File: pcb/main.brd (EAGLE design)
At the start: 160 x 100 mm, 45 parts, among them IC1 FT230XS, J3 455-1750-1-ND, J6 M1 connector, J7 M2 connector, Q1 2.5A/30V/105mΩ, U1 LSM303C, U2 ESP-WROOM-32

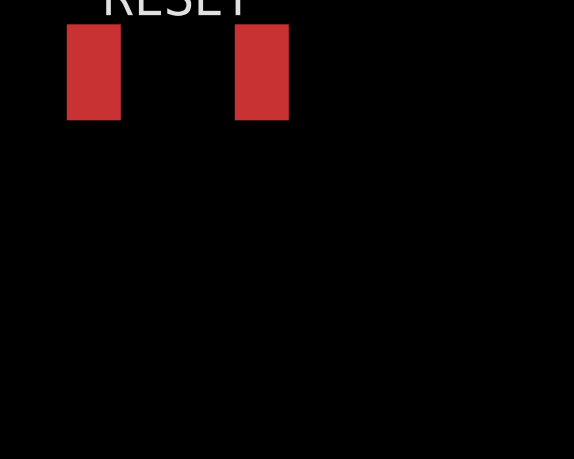
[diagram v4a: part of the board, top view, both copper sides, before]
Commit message: mosfet for laser
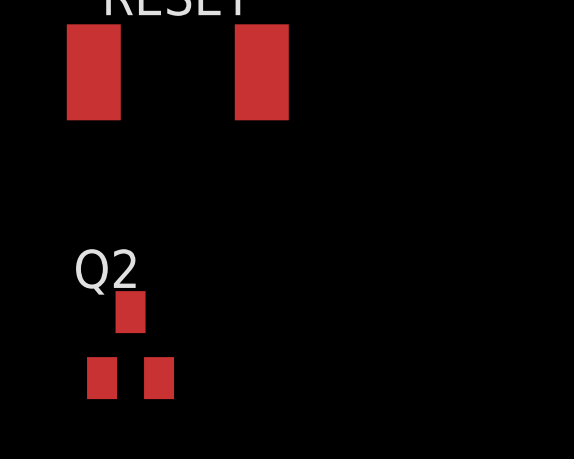
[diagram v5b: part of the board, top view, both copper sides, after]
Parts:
- added Q2: (no value), adafruit:SOT23
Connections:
- new net N$10: J2.1, Q2.3
- net 5V: now also J2.2
- net GND: now also Q2.2; no longer J2.1
- net PWM_LASER: now also Q2.1; no longer J2.2
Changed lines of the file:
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@@
 <element name="CN1" library="adafruit" library_urn="urn:adsk.eagle:library:420" package="USB-MINIB" value="" x="-101.9556" y="-131.8768"/>
 <element name="RESET" library="DiscreteComponents" package="SW_2512" value="" x="-103.4288" y="-144.0688"/>
+<element name="Q2" library="adafruit" library_urn="urn:adsk.eagle:library:420" package="SOT23" value="" x="-105.0036" y="-153.162"/>
 </elements>
 <signals>
@@
 <contactref element="J3" pad="3"/>
 <contactref element="J1" pad="1"/>
-<contactref element="J2" pad="1"/>
 <contactref element="D2" pad="C"/>
 <contactref element="R1" pad="1"/>
@@
 <contactref element="CN1" pad="GND"/>
 <contactref element="RESET" pad="2"/>
+<contactref element="Q2" pad="2"/>
+<wire x1="-104.0536" y1="-154.262" x2="-100.6288" y2="-144.0688" width="0" layer="19" extent="1-1"/>
 <wire x1="-100.3556" y1="-127.8128" x2="-100.6288" y2="-144.0688" width="0" layer="19" extent="1-1"/>
 <wire x1="-91.86" y1="-117.348" x2="-100.3556" y2="-127.8128" width="0" layer="19" extent="1-1"/>
@@
 <wire x1="-33.413" y1="53.34" x2="-30.48" y2="49.53" width="0" layer="19" extent="1-1"/>
 <wire x1="-36.83" y1="49.53" x2="-33.413" y2="53.34" width="0" layer="19" extent="1-1"/>
-<wire x1="-24.13" y1="49.53" x2="-30.48" y2="49.53" width="0" layer="19" extent="1-1"/>
-<wire x1="-17.78" y1="49.53" x2="-24.13" y2="49.53" width="0" layer="19" extent="1-1"/>
+<wire x1="-46.14" y1="49.53" x2="-36.83" y2="49.53" width="0" layer="19" extent="1-1"/>
+<wire x1="-20.0914" y1="40.0812" x2="-30.775" y2="38.985" width="0" layer="19" extent="1-1"/>
+<wire x1="-21.59" y1="33.02" x2="-20.0914" y2="40.0812" width="0" layer="19" extent="1-1"/>
+<wire x1="-17.78" y1="49.53" x2="-20.0914" y2="40.0812" width="0" layer="19" extent="1-1"/>
 <wire x1="-19.9" y1="54.61" x2="-17.78" y2="49.53" width="0" layer="19" extent="1-1"/>
 <wire x1="-14.39" y1="54.61" x2="-19.9" y2="54.61" width="0" layer="19" extent="1-1"/>
-<wire x1="-46.14" y1="49.53" x2="-36.83" y2="49.53" width="0" layer="19" extent="1-1"/>
-<wire x1="-20.0914" y1="40.0812" x2="-17.78" y2="49.53" width="0" layer="19" extent="1-1"/>
-<wire x1="-21.59" y1="33.02" x2="-20.0914" y2="40.0812" width="0" layer="19" extent="1-1"/>
 <wire x1="-21.59" y1="23.12" x2="-21.59" y2="33.02" width="0" layer="19" extent="1-1"/>
 <wire x1="-18.19" y1="23.12" x2="-21.59" y2="23.12" width="0" layer="19" extent="1-1"/>
@@
 </signal>
 <signal name="PWM_LASER">
-<contactref element="J2" pad="2"/>
+<contactref element="Q2" pad="1"/>
 </signal>
 <signal name="5V">
@@
 <contactref element="U$1" pad="2"/>
 <contactref element="U$1" pad="4"/>
-<wire x1="-17.78" y1="46.279" x2="-16.09" y2="54.61" width="0" layer="19" extent="1-1"/>
+<contactref element="J2" pad="2"/>
+<wire x1="-21.59" y1="49.53" x2="-16.09" y2="54.61" width="0" layer="19" extent="1-1"/>
+<wire x1="-17.78" y1="46.279" x2="-21.59" y2="49.53" width="0" layer="19" extent="1-1"/>
 <wire x1="-17.78" y1="40.0812" x2="-17.78" y2="46.279" width="0" layer="19" extent="1-1"/>
-<wire x1="-39.37" y1="40.64" x2="-17.78" y2="40.0812" width="0" layer="19" extent="1-1"/>
+<wire x1="-39.37" y1="40.64" x2="-21.59" y2="49.53" width="0" layer="19" extent="1-1"/>
 </signal>
 <signal name="PWM_SERVO">
@@
 <contactref element="IC1" pad="6"/>
 </signal>
+<signal name="N$10">
+<contactref element="Q2" pad="3"/>
+<contactref element="J2" pad="1"/>
+<wire x1="-105.0036" y1="-152.062" x2="-24.13" y2="49.53" width="0" layer="19" extent="1-1"/>
+</signal>
 </signals>

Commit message: wired up almost all of esp's peripherals
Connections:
- new net ADC_PHOTO: J4.2, R3.1, U2.35
- new net N$16: U2.26
- new net RST: U2.3
- new net TCK: U2.16
- new net TDI: U2.14
- new net TDO: U2.23
- new net TMS: U2.13
- net M1+: now also U2.8
- net M1-: now also U2.9
- net M2+: now also U2.10
- net M2-: now also U2.11
- net N$4: now also U2.25; no longer J4.2, R3.1
- net PWM_LASER: now also U2.24
- net PWM_LED: now also U2.34
- net PWM_SERVO: now also U2.12
- net SCL: now also U2.36
- net SDA: now also U2.33
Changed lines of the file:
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@@
 <?xml version="1.0" encoding="utf-8"?>
 <!DOCTYPE eagle SYSTEM "eagle.dtd">
-<eagle version="8.3.2">
+<eagle version="8.6.0">
 <drawing>
 <settings>
@@
 <param name="dpMaxLengthDifference" value="10mm"/>
 <param name="dpGapFactor" value="2.5"/>
-<param name="checkGrid" value="0"/>
 <param name="checkAngle" value="0"/>
 <param name="checkFont" value="1"/>
 <param name="checkRestrict" value="1"/>
+<param name="checkStop" value="0"/>
+<param name="checkValues" value="0"/>
 <param name="useDiameter" value="13"/>
 <param name="maxErrors" value="50"/>
@@
 </element>
 <element name="J8" library="electricSheepParty" package="1X02" value="" x="-87.0204" y="-129.3368">
-<attribute name="COMM" value="Photo Receptor" x="-87.0204" y="-129.3368" size="1.778" layer="27" display="off"/>
+<attribute name="COMM" value="IMU Interrupt Header" x="-87.0204" y="-129.3368" size="1.778" layer="27" display="off"/>
 </element>
 <element name="CN1" library="adafruit" library_urn="urn:adsk.eagle:library:420" package="USB-MINIB" value="" x="-101.9556" y="-131.8768"/>
@@
 <signal name="PWM_LASER">
 <contactref element="Q2" pad="1"/>
+<contactref element="U2" pad="24"/>
+<wire x1="-105.9536" y1="-154.262" x2="-77.9376" y2="-98.7276" width="0" layer="19" extent="1-1"/>
 </signal>
 <signal name="5V">
@@
 <signal name="PWM_SERVO">
 <contactref element="J3" pad="1"/>
+<contactref element="U2" pad="12"/>
+<wire x1="-41.91" y1="40.64" x2="-92.9176" y2="-94.4476" width="0" layer="19" extent="1-1"/>
 </signal>
 <signal name="N$1">
@@
 <wire x1="-35.167" y1="53.34" x2="-23.71" y2="54.61" width="0" layer="19" extent="1-1"/>
 </signal>
-<signal name="N$4">
+<signal name="ADC_PHOTO">
 <contactref element="J4" pad="2"/>
 <contactref element="R3" pad="1"/>
-<wire x1="-27.94" y1="49.53" x2="-27.52" y2="54.61" width="0" layer="19" extent="1-1"/>
+<contactref element="U2" pad="35"/>
+<wire x1="-27.94" y1="49.53" x2="-74.4176" y2="-84.2876" width="0" layer="19" extent="1-1"/>
+<wire x1="-27.52" y1="54.61" x2="-27.94" y2="49.53" width="0" layer="19" extent="1-1"/>
 </signal>
 <signal name="N$5">
@@
 <signal name="PWM_LED">
 <contactref element="R4" pad="2"/>
+<contactref element="U2" pad="34"/>
+<wire x1="-29.63" y1="54.61" x2="-74.4176" y2="-85.5576" width="0" layer="19" extent="1-1"/>
 </signal>
 <signal name="3V3">
@@
 <contactref element="U$2" pad="2"/>
 <contactref element="J6" pad="2"/>
+<contactref element="U2" pad="8"/>
+<wire x1="-39.37" y1="-30.48" x2="-92.9176" y2="-89.3676" width="0" layer="19" extent="1-1"/>
 <wire x1="-33.375" y1="38.985" x2="-39.37" y2="-30.48" width="0" layer="19" extent="1-1"/>
 </signal>
@@
 <contactref element="U$2" pad="4"/>
 <contactref element="J6" pad="1"/>
+<contactref element="U2" pad="9"/>
+<wire x1="-41.91" y1="-30.48" x2="-92.9176" y2="-90.6376" width="0" layer="19" extent="1-1"/>
 <wire x1="-32.075" y1="38.985" x2="-41.91" y2="-30.48" width="0" layer="19" extent="1-1"/>
 </signal>
@@
 <contactref element="U$2" pad="7"/>
 <contactref element="J7" pad="2"/>
+<contactref element="U2" pad="10"/>
+<wire x1="-39.37" y1="-49.53" x2="-92.9176" y2="-91.9076" width="0" layer="19" extent="1-1"/>
 <wire x1="-30.125" y1="38.985" x2="-39.37" y2="-49.53" width="0" layer="19" extent="1-1"/>
 </signal>
@@
 <contactref element="U$2" pad="5"/>
 <contactref element="J7" pad="1"/>
+<contactref element="U2" pad="11"/>
+<wire x1="-41.91" y1="-49.53" x2="-92.9176" y2="-93.1776" width="0" layer="19" extent="1-1"/>
 <wire x1="-31.425" y1="38.985" x2="-41.91" y2="-49.53" width="0" layer="19" extent="1-1"/>
 </signal>
@@
 <signal name="SCL">
 <contactref element="U1" pad="1"/>
+<contactref element="U2" pad="36"/>
+<wire x1="-74.4176" y1="-83.0176" x2="-70.6508" y2="-98.8688" width="0" layer="19" extent="1-1"/>
 </signal>
 <signal name="SDA">
 <contactref element="U1" pad="4"/>
+<contactref element="U2" pad="33"/>
+<wire x1="-74.4176" y1="-86.8276" x2="-70.6508" y2="-100.3688" width="0" layer="19" extent="1-1"/>
 </signal>
 <signal name="N$12">
@@
 <wire x1="-105.0036" y1="-152.062" x2="-24.13" y2="49.53" width="0" layer="19" extent="1-1"/>
 </signal>
+<signal name="TDI">
+<contactref element="U2" pad="14"/>
+</signal>
+<signal name="TMS">
+<contactref element="U2" pad="13"/>
+</signal>
+<signal name="TDO">
+<contactref element="U2" pad="23"/>
+</signal>
+<signal name="TCK">
+<contactref element="U2" pad="16"/>
+</signal>
+<signal name="RST">
+<contactref element="U2" pad="3"/>
+</signal>
+<signal name="N$16">
+<contactref element="U2" pad="26"/>
+</signal>
+<signal name="N$4">
+<contactref element="U2" pad="25"/>
+</signal>
 </signals>

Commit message: more esp pins and isolating grounds
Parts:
- removed CN1: (no value), adafruit:USB-MINIB
- removed IC1: FT230XS, electricSheepParty:SSOP16
- removed J8: (no value), electricSheepParty:1X02
- removed RESET: (no value), DiscreteComponents:SW_2512
- added C15: 10uF, rcl:C0805
- added C16, C17: 1nF, electricSheepParty:0603
- added C18, C20: 100uF, eagle-ltspice:C1206
- added C19: 1uF, electricSheepParty:0603
- added FB1: (no value), rcl:R0603
- added R10: 470, electricSheepParty:0603
- added R8: 20k, electricSheepParty:0603
- added R9: 10k, electricSheepParty:0603
- added RESET1: S2, DiscreteComponents:SW_2512
- C14: device electricSheepParty:0603 -> rcl:C0805
- C3, C5: device rcl:C0603 -> rcl:C0805
- R1: value 100k -> 1M
- R3, R5: value (none) -> 10k
- R4: value (none) -> 470
- moved R4 260.5 mm to (-121.8, -189.4)
- moved C3 180.2 mm to (-105.4, -178.5)
- moved C5 176.4 mm to (-105.4, -184.7)
- moved D1 72.7 mm to (22.6, 15.9)
- moved C14 56.5 mm to (-105.4, -172.4)
- moved Q1 55.8 mm to (22.6, 13.4), turned to 180 degrees
- moved R1 48.6 mm to (15.9, 20.8)
- moved J1 47.3 mm to (12.4, 13.1), turned to 270 degrees
- moved S1 46.2 mm to (16.5, 4.27), turned to 270 degrees
- renumbered U2 to U5
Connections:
- net N$4 renamed IO0
- removed net CTS: IC1.6
- removed net D+: CN1.D+, IC1.8
- removed net D-: CN1.D-, IC1.9
- removed net RESET: IC1.11, RESET.1
- removed net RST: U5.3
- removed net RTS: IC1.2
- removed net RX: IC1.4
- removed net TX: IC1.1
- new net 1/3_BAT: R8.1, R9.2, U5.4
- new net 6V_RAW: J1.2, S1.P$2
- new net AGND: C1.2, C10.-, C11.2, C15.1, C2.2, C20.2, C3.2, C4.2, C6.2, C7.2, C8.2, C9.-, D2.C, D3.1, FB1.1, J1.1, J3.3, Q2.2, R1.1, R9.1, U$1.1, U$2.13, U$2.17, U$2.3, U$2.6, U$3.3, U$3.5, U$3.6
- new net EN: C17.1, R10.2, R4.2, U5.3
- new net N$11: C16.1, R4.1, RESET1.1
- new net N$14: U5.7
- new net N$15: U5.20
- new net N$17: U5.21
- new net N$18: U5.22
- new net N$19: U5.27
- new net N$23: U5.31
- new net N$24: U5.37
- new net N$4: U5.5
- new net PHOTO: U5.35
- net 3V3: now also C20.1, C5.1, R10.1; no longer C5.2, CN1.VBUS, IC1.10, IC1.12, IC1.3, U5.2
- net 5V: now also C15.2
- net 6V: now also D1.C, Q1.2, R2.2, R8.2
- net ADC_PHOTO: no longer U5.35
- net GND: now also C16.2, C17.2, C18.2, C19.2, FB1.2, RESET1.2; no longer C1.2, C10.-, C11.2, C2.2, C3.2, C4.2, C6.2, C7.2, C8.2, C9.-, CN1.GND, D2.C, D3.1, IC1.13, IC1.5, J1.1, J3.3, Q2.2, R1.1, RESET.2, U$1.1, U$2.13, U$2.17, U$2.3, U$2.6, U$3.3, U$3.5, U$3.6
- net INT_MAG: now also U5.29; no longer J8.1
- net INT_XL: now also U5.30; no longer J8.2
- net M1+: no longer U5.8
- net M1-: no longer U5.9
- net M2+: no longer U5.10
- net M2-: no longer U5.11
- net MAG_RDY: now also U5.28
- net N$5: now also U5.6; no longer J5.2, R4.1
- net N$9: now also C5.2; no longer C5.1
- net PWM_LED: now also J5.2; no longer R4.2
- net PWM_M1A: now also U5.8
- net PWM_M1B: now also U5.9
- net PWM_M2A: now also U5.11
- net PWM_M2B: now also U5.10
- net VCC: now also C18.1, C19.1, U5.2; no longer D1.C, J1.2, Q1.2, R2.2, S1.P$2
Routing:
- added copper zone on layer 1, net 6V_RAW
- added copper zone on layer 1, net N$3

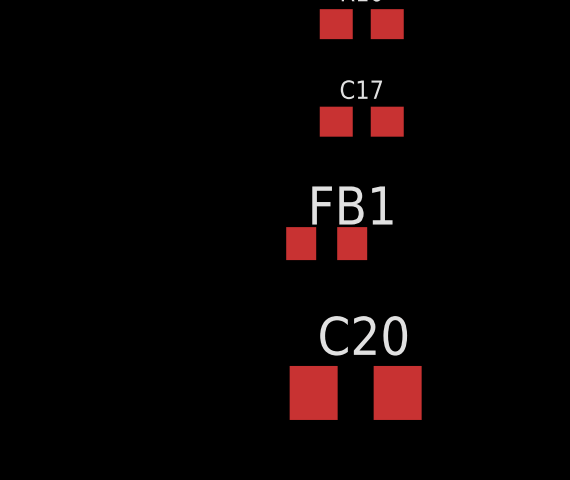
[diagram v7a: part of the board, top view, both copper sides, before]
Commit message: added schmitt trigger
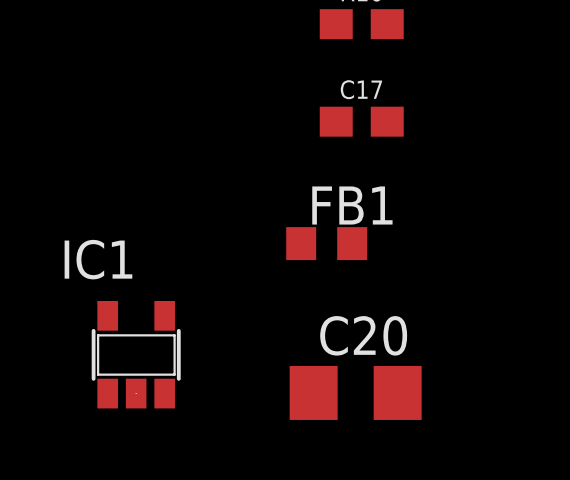
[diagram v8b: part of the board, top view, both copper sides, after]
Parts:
- added IC1: NC7SZ14M5X, electricSheepParty:SOT23-5
- R3: value 10k -> 8.2k
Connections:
- net ADC_PHOTO: now also IC1.2
- net GND: now also IC1.3
- net PHOTO: now also IC1.4
- net VCC: now also IC1.5
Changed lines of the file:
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@@
 <?xml version="1.0" encoding="utf-8"?>
 <!DOCTYPE eagle SYSTEM "eagle.dtd">
-<eagle version="8.3.2">
+<eagle version="8.6.0">
 <drawing>
 <settings>
@@
 <param name="dpMaxLengthDifference" value="10mm"/>
 <param name="dpGapFactor" value="2.5"/>
-<param name="checkGrid" value="0"/>
 <param name="checkAngle" value="0"/>
 <param name="checkFont" value="1"/>
 <param name="checkRestrict" value="1"/>
+<param name="checkStop" value="0"/>
+<param name="checkValues" value="0"/>
 <param name="useDiameter" value="13"/>
 <param name="maxErrors" value="50"/>
@@
 <attribute name="PROD_ID" value=" " x="-22.86" y="54.61" size="1.778" layer="27" display="off"/>
 </element>
-<element name="R3" library="electricSheepParty" package="0603" value="10k" x="-26.67" y="54.61">
+<element name="R3" library="electricSheepParty" package="0603" value="8.2k" x="-26.67" y="54.61">
 <attribute name="PROD_ID" value=" " x="-26.67" y="54.61" size="1.778" layer="27" display="off"/>
 </element>
@@
 <attribute name="SPICEPREFIX" value="C" x="-121.9708" y="-224.028" size="1.778" layer="27" display="off"/>
 </element>
+<element name="IC1" library="electricSheepParty" package="SOT23-5" value="NC7SZ14M5X" x="-129.286" y="-222.758"/>
 </elements>
 <signals>
@@
 <contactref element="C17" pad="2"/>
 <contactref element="FB1" pad="2"/>
+<contactref element="IC1" pad="3"/>
 <wire x1="-91.86" y1="-110.8456" x2="-91.86" y2="-114.0968" width="0" layer="19" extent="1-1"/>
 <wire x1="-93.56" y1="-104.3432" x2="-91.86" y2="-110.8456" width="0" layer="19" extent="1-1"/>
@@
 <wire x1="-120.9176" y1="-214.9856" x2="-120.9176" y2="-208.4832" width="0" layer="19" extent="1-1"/>
 <wire x1="-122.086" y1="-219.0496" x2="-120.9176" y2="-214.9856" width="0" layer="19" extent="1-1"/>
+<wire x1="-128.336" y1="-224.048" x2="-122.086" y2="-219.0496" width="0" layer="19" extent="1-1"/>
 <wire x1="-36.83" y1="49.53" x2="-74.4176" y2="-80.4776" width="0" layer="19" extent="1-1"/>
 <wire x1="-30.48" y1="49.53" x2="-36.83" y2="49.53" width="0" layer="19" extent="1-1"/>
@@
 <contactref element="J4" pad="2"/>
 <contactref element="R3" pad="1"/>
-<wire x1="-27.94" y1="49.53" x2="-27.52" y2="54.61" width="0" layer="19" extent="1-1"/>
+<contactref element="IC1" pad="2"/>
+<wire x1="-27.94" y1="49.53" x2="-129.286" y2="-224.048" width="0" layer="19" extent="1-1"/>
+<wire x1="-27.52" y1="54.61" x2="-27.94" y2="49.53" width="0" layer="19" extent="1-1"/>
 </signal>
 <signal name="PWM_LED">
@@
 <vertex x="9.8044" y="11.7348"/>
 </polygon>
+<wire x1="16.4592" y1="4.2672" x2="12.3952" y2="10.5664" width="0" layer="19" extent="1-1"/>
 </signal>
 <signal name="1/3_BAT">
@@
 <contactref element="C18" pad="1"/>
 <contactref element="C19" pad="1"/>
+<contactref element="IC1" pad="5"/>
 <wire x1="-123.3708" y1="-203.8096" x2="-92.9176" y2="-81.7476" width="0" layer="19" extent="1-1"/>
 <wire x1="-122.6176" y1="-208.4832" x2="-123.3708" y2="-203.8096" width="0" layer="19" extent="1-1"/>
+<wire x1="-130.236" y1="-221.458" x2="-122.6176" y2="-208.4832" width="0" layer="19" extent="1-1"/>
 </signal>
 <signal name="EN">
@@
 <signal name="PHOTO">
 <contactref element="U5" pad="35"/>
+<contactref element="IC1" pad="4"/>
+<wire x1="-128.336" y1="-221.458" x2="-74.4176" y2="-84.2876" width="0" layer="19" extent="1-1"/>
 </signal>
 <signal name="AGND">
